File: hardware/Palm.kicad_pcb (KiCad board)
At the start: 2 copper layers, 10 parts, among them J1 Conn_01x02_Female, Q1 IRLML6402, SW1 SW_SPDT, SW2 SW_SPDT, U1 Adafruit_nRF52_Feather, U2 VEML6075_breakout

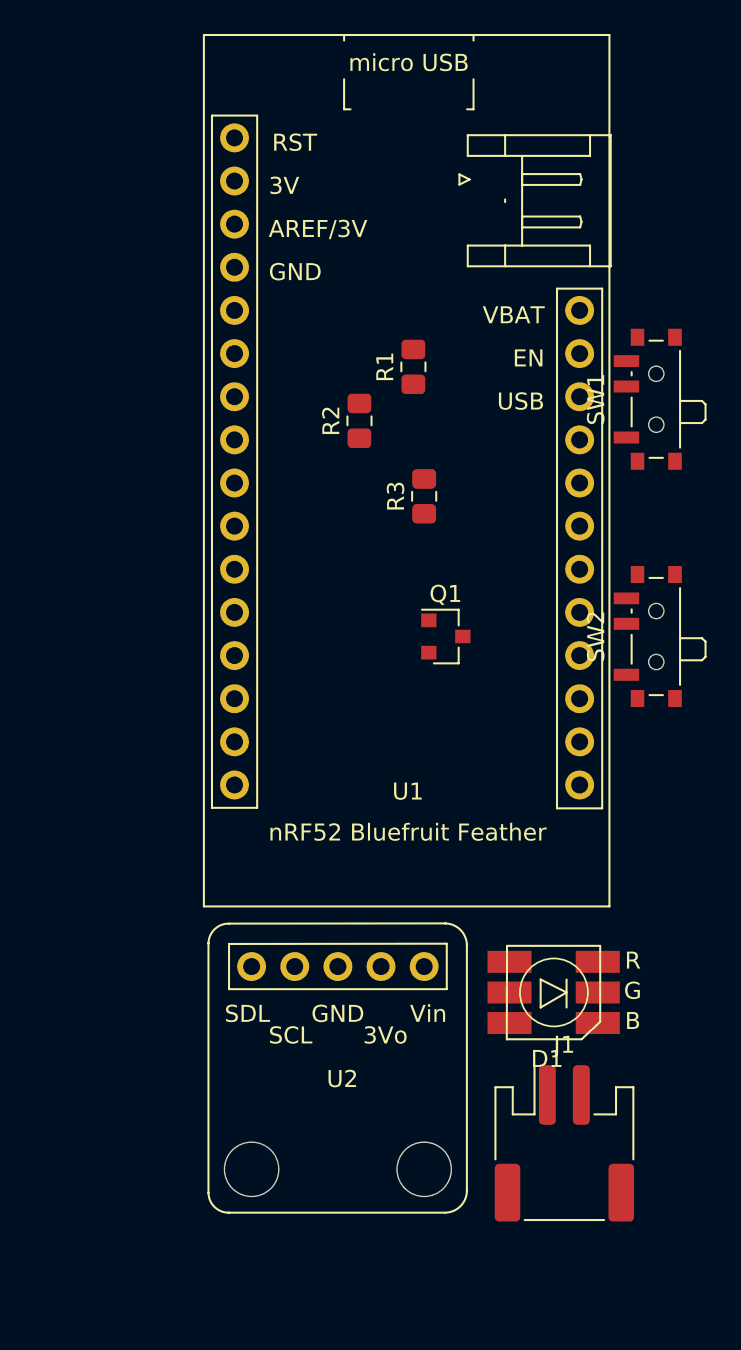
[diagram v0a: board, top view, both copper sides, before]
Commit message: [footprint] Add rats net
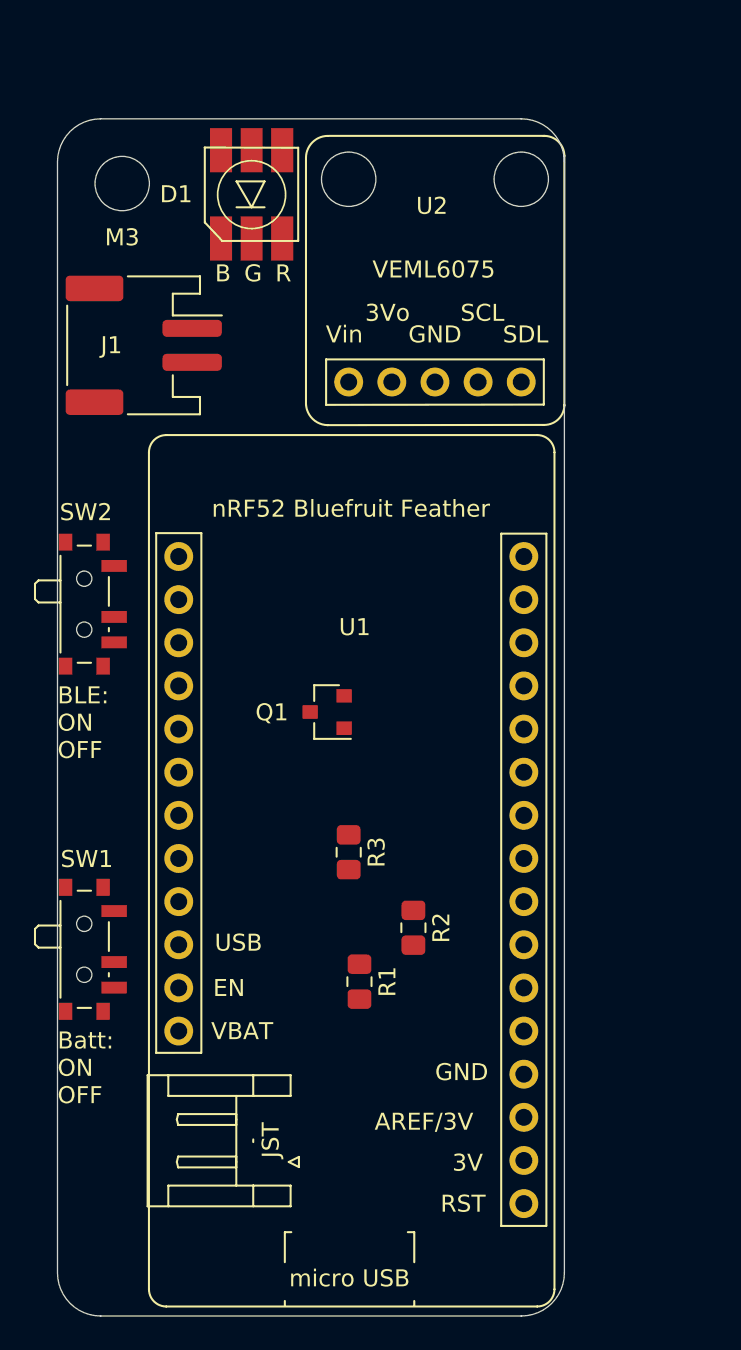
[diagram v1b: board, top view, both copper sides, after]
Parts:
- added M3: Keychain hole, MountingHole:MountingHole_3.2mm_M3, F.Cu at (134.0, 55.2)
- J1: value Conn_01x02_Female -> JST PH2
- moved J1 53.1 mm to (135.3, 64.8), turned to 270 degrees
- moved D1 50.2 mm to (141.6, 55.9), turned to 90 degrees
- moved SW1 46.3 mm to (132.1, 100.3), turned to 270 degrees
- moved U2 45.4 mm to (152.4, 61.6), turned to 0 degrees
- moved R1 36.3 mm to (148.0, 102.2), turned to 270 degrees
- moved SW2 33.1 mm to (132.1, 80.0), turned to 270 degrees
- moved R2 30.0 mm to (151.1, 99.1), turned to 270 degrees
- moved U1 23.9 mm to (147.0, 95.7), turned to 180 degrees
- moved R3 21.4 mm to (147.3, 94.6), turned to 270 degrees
- moved Q1 8.28 mm to (146.1, 86.4), turned to 180 degrees
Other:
- board outline added: 29.8 x 70.5 mm
- board text added: "BLE: ON OFF"
- board text added: "Batt: ON OFF"

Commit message: [footprint] Add back Cu zone with GND
Co-authored-by: Chinmay Pendharkar <notthetup@gmail.com>
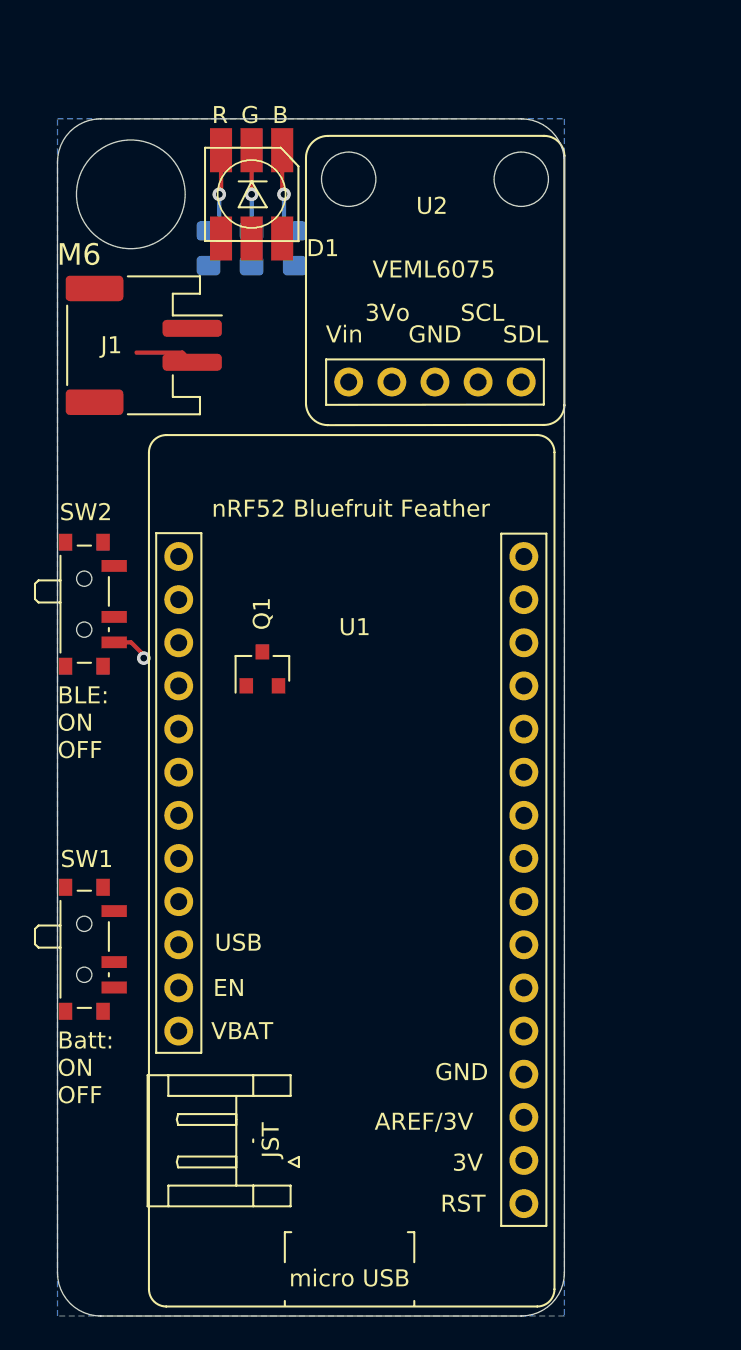
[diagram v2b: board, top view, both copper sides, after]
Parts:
- removed M3: Keychain hole, MountingHole:MountingHole_3.2mm_M3
- added M6: , , F.Cu at (140.0, 57.5)
- R1, R2, R3: moved to B.Cu
- moved R1 43.3 mm to (144.1, 59.1)
- moved R2 41.1 mm to (141.6, 59.1)
- moved R3 36.5 mm to (139.1, 59.1)
- moved Q1 4.58 mm to (142.2, 83.8), turned to 90 degrees
- turned D1 to 270 degrees
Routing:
- net GND: track 0.00 -> 5.75 mm, vias 0 -> 1
- net Net-(D1-Pad3): track 0.00 -> 5.06 mm, vias 0 -> 1
- net Net-(D1-Pad1): track 0.00 -> 5.06 mm, vias 0 -> 1
- net Net-(D1-Pad2): track 0.00 -> 4.75 mm, vias 0 -> 1
- added copper zone on B.Cu, net GND

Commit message: [footprint] Link SDA/SCL and RGB LED tracks
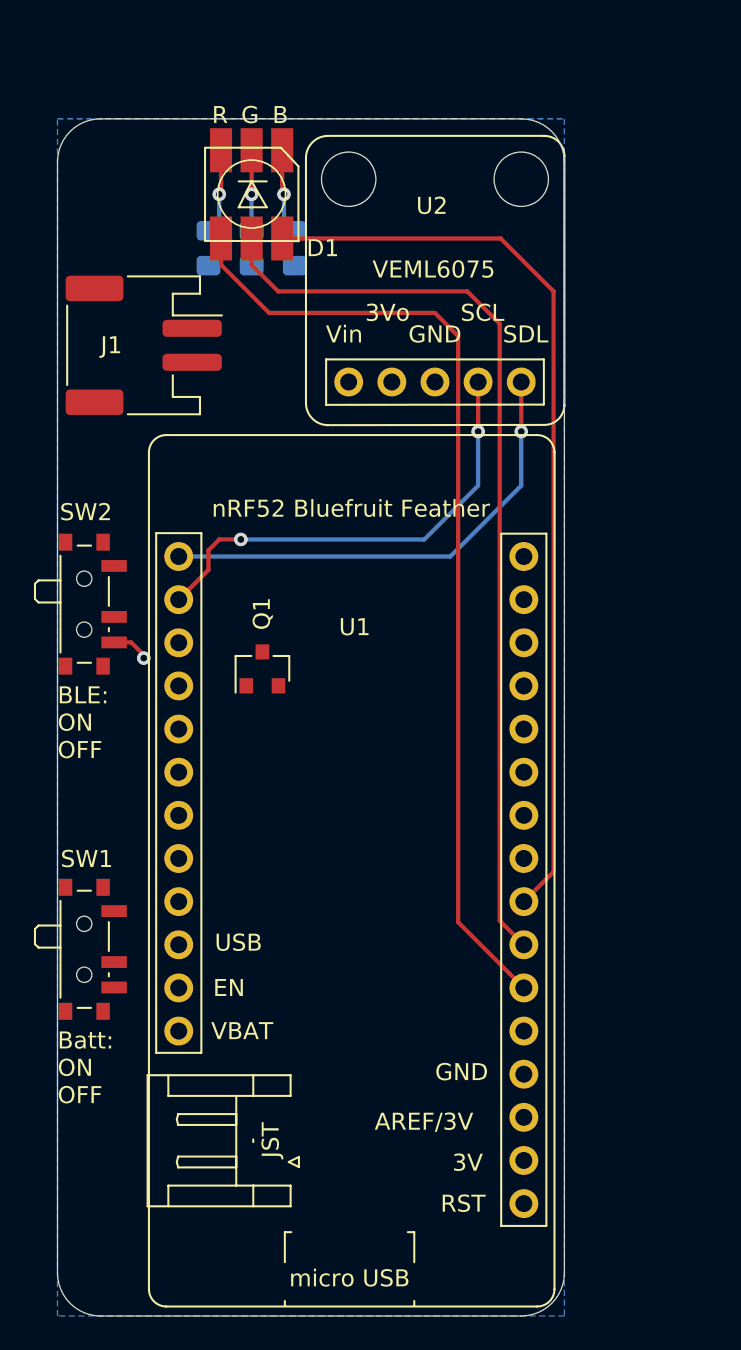
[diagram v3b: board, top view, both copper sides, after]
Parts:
- removed M6: , 
- J1: value JST PH2 -> Conn_01x02_Female
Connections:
- SW1 pad 3: Net-(SW1-Pad3) -> (no net)
- U1 pad 1: Net-(U1-Pad1) -> (no net)
- U1 pad 10: Net-(U1-Pad10) -> (no net)
- U1 pad 11: Net-(U1-Pad11) -> (no net)
- U1 pad 12: Net-(U1-Pad12) -> (no net)
- U1 pad 13: Net-(U1-Pad13) -> (no net)
- U1 pad 14: Net-(U1-Pad14) -> (no net)
- U1 pad 15: Net-(U1-Pad15) -> (no net)
- U1 pad 16: Net-(U1-Pad16) -> (no net)
- U1 pad 19: Net-(U1-Pad19) -> (no net)
- U1 pad 20: Net-(U1-Pad20) -> (no net)
- U1 pad 21: Net-(U1-Pad21) -> (no net)
- U1 pad 22: Net-(U1-Pad22) -> (no net)
- U1 pad 23: Net-(U1-Pad23) -> (no net)
- U1 pad 26: +5V -> (no net)
- U1 pad 27: Net-(U1-Pad27) -> (no net)
- U1 pad 3: Net-(U1-Pad3) -> (no net)
- U1 pad 5: Net-(U1-Pad5) -> (no net)
- U1 pad 6: /RED -> /BLUE
- U1 pad 8: /BLUE -> /RED
- U1 pad 9: Net-(U1-Pad9) -> (no net)
- U2 pad 2: Net-(U2-Pad2) -> (no net)
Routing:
- net /BLUE: track 0.00 -> 57.2 mm
- net /GREEN: track 0.00 -> 54.7 mm
- net /RED: track 0.00 -> 53.9 mm
- net /SDA: track 0.00 -> 28.0 mm, vias 0 -> 1
- net /SCL: track 0.00 -> 27.2 mm, vias 0 -> 2
- net GND: track 5.75 -> 2.23 mm

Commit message: [footprint] Complete footprint layout
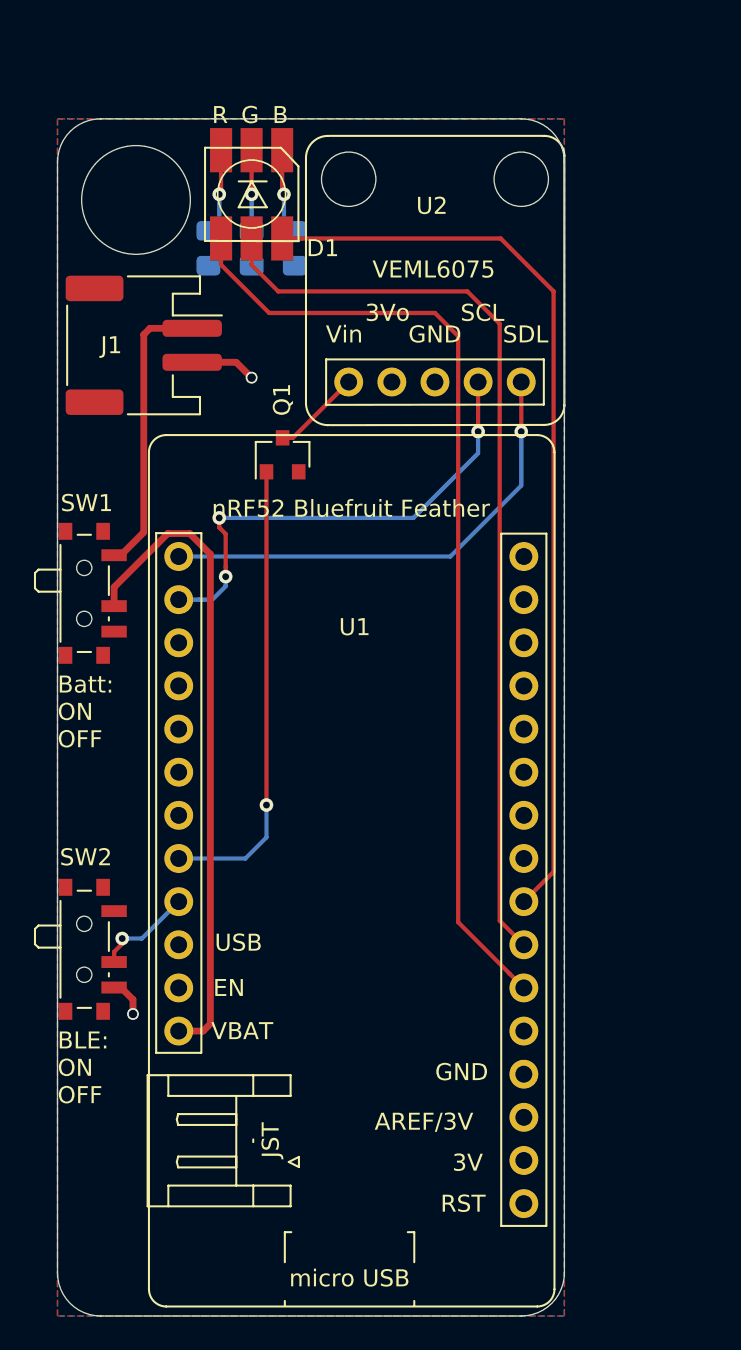
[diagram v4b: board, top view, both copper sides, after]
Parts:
- added ?: , , F.Cu at (135.9, 56.5)
- moved SW1 21.0 mm to (132.1, 79.4)
- moved SW2 20.3 mm to (132.1, 100.3)
- moved Q1 12.7 mm to (143.4, 71.2)
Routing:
- net Net-(SW1-Pad2): track 0.00 -> 38.3 mm
- net /EN_SENSOR: track 0.00 -> 27.2 mm, vias 0 -> 1
- net Net-(J1-Pad1): track 0.00 -> 16.9 mm
- net Net-(SW2-Pad2): track 0.00 -> 5.81 mm, vias 0 -> 1
- net Net-(Q1-Pad3): track 0.00 -> 5.25 mm
- net GND: track 2.23 -> 6.13 mm, vias 1 -> 2
- net /SCL: track 27.2 -> 28.4 mm, vias 2 -> 3
- added copper zone on F.Cu, net +3V3
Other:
- net class Power added: clearance 0.3, trace_width 0.4, via_dia 0.7, via_drill 0.5

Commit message: [footprint] Update footprint layout
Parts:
- moved R1 2.54 mm to (144.1, 61.6)
- moved R2 2.54 mm to (141.6, 61.6)
- moved R3 2.54 mm to (139.1, 61.6)
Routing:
- net Net-(D1-Pad3): track 5.06 -> 7.60 mm
- net Net-(D1-Pad2): track 4.75 -> 7.29 mm
- net Net-(D1-Pad1): track 5.06 -> 7.60 mm
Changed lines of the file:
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@@
     (thickness 1.6)
     (drawings 12)
-    (tracks 83)
+    (tracks 86)
     (zones 0)
     (modules 11)
@@
   )
   (page A4)
+  (title_block
+    (title Palm@Hutscape)
+    (date 2019-06-10)
+    (rev V1.0)
+    (comment 1 "Keychain for measuring UV Index")
+  )
   (layers
     (0 F.Cu signal)
     (31 B.Cu signal)
-    (32 B.Adhes user hide)
+    (32 B.Adhes user)
     (33 F.Adhes user)
-    (34 B.Paste user hide)
+    (34 B.Paste user)
     (35 F.Paste user)
-    (36 B.SilkS user hide)
+    (36 B.SilkS user)
     (37 F.SilkS user)
     (38 B.Mask user)
@@
     (44 Edge.Cuts user)
     (45 Margin user)
-    (46 B.CrtYd user hide)
-    (47 F.CrtYd user hide)
-    (48 B.Fab user hide)
-    (49 F.Fab user hide)
+    (46 B.CrtYd user)
+    (47 F.CrtYd user)
+    (48 B.Fab user)
+    (49 F.Fab user)
   )
   (setup
@@
     (solder_mask_min_width 0.25)
     (aux_axis_origin 74.93 106.045)
-    (visible_elements FFFFFF7F)
+    (visible_elements FFFFFFFF)
     (pcbplotparams
       (layerselection 0x010fc_ffffffff)
@@
     (fp_arc (start 10.414 -24.638) (end 11.43 -24.638) (angle -90) (layer F.SilkS) (width 0.12))
     (fp_arc (start -11.43 -24.638) (end -11.43 -25.654) (angle -90) (layer F.SilkS) (width 0.12))
-    (fp_text user JST (at 4.2545 -15.8623 270) (layer F.SilkS)
+    (fp_text user JST (at 3.4798 -16.0528) (layer F.SilkS)
       (effects (font (size 1 1) (thickness 0.15)))
     )
@@
       (effects (font (size 1 1) (thickness 0.15)))
     )
-    (fp_text user B (at -4.6609 -1.6891) (layer F.SilkS)
-      (effects (font (size 1 1) (thickness 0.15)))
-    )
-    (fp_text user G (at -4.6609 0.0889) (layer F.SilkS)
-      (effects (font (size 1 1) (thickness 0.15)))
-    )
-    (fp_text user R (at -4.6609 1.8669) (layer F.SilkS)
+    (fp_text user B (at -0.508 -1.651) (layer F.SilkS)
+      (effects (font (size 1 1) (thickness 0.15)))
+    )
+    (fp_text user R (at -0.508 1.905) (layer F.SilkS)
       (effects (font (size 1 1) (thickness 0.15)))
     )
@@
   )
   (module Resistor_SMD:R_0805_2012Metric_Pad1.15x1.40mm_HandSolder (layer B.Cu)
-    (at 139.065 59.055 270)
+    (at 139.065 61.595 270)
     (descr "Resistor SMD 0805 (2012 Metric), square (rectangular) end terminal, IPC_7351 nominal with elongated pad for handsoldering. (Body size source: https://docs.google.com/spreadsheets/d/1BsfQQcO9C6DZCsRaXUlFlo91Tg2WpOkGARC1WS5S8t0/edit?usp=sharing), generated with kicad-footprint-generator")
     (tags "resistor handsolder")
     (attr smd)
-    (fp_text reference R3 (at 0 -1.905) (layer B.SilkS)
+    (fp_text reference R3 (at 2.54 0) (layer B.SilkS)
       (effects (font (size 1 1) (thickness 0.15)) (justify mirror))
     )
@@
   )
   (module Resistor_SMD:R_0805_2012Metric_Pad1.15x1.40mm_HandSolder (layer B.Cu)
-    (at 141.605 59.055 270)
+    (at 141.605 61.595 270)
     (descr "Resistor SMD 0805 (2012 Metric), square (rectangular) end terminal, IPC_7351 nominal with elongated pad for handsoldering. (Body size source: https://docs.google.com/spreadsheets/d/1BsfQQcO9C6DZCsRaXUlFlo91Tg2WpOkGARC1WS5S8t0/edit?usp=sharing), generated with kicad-footprint-generator")
     (tags "resistor handsolder")
     (attr smd)
-    (fp_text reference R2 (at 0 -1.905) (layer B.SilkS)
+    (fp_text reference R2 (at 2.54 0) (layer B.SilkS)
       (effects (font (size 1 1) (thickness 0.15)) (justify mirror))
     )
@@
   )
   (module Resistor_SMD:R_0805_2012Metric_Pad1.15x1.40mm_HandSolder (layer B.Cu)
-    (at 144.145 59.055 270)
+    (at 144.145 61.595 270)
     (descr "Resistor SMD 0805 (2012 Metric), square (rectangular) end terminal, IPC_7351 nominal with elongated pad for handsoldering. (Body size source: https://docs.google.com/spreadsheets/d/1BsfQQcO9C6DZCsRaXUlFlo91Tg2WpOkGARC1WS5S8t0/edit?usp=sharing), generated with kicad-footprint-generator")
     (tags "resistor handsolder")
     (attr smd)
-    (fp_text reference R1 (at 0 -1.905) (layer B.SilkS)
+    (fp_text reference R1 (at 2.54 0) (layer B.SilkS)
       (effects (font (size 1 1) (thickness 0.15)) (justify mirror))
     )
@@
     (tags SOT-23)
     (attr smd)
-    (fp_text reference Q1 (at 3.2512 -0.0254 90) (layer F.SilkS)
+    (fp_text reference Q1 (at 2.63652 -0.0254 180) (layer F.SilkS)
       (effects (font (size 1 1) (thickness 0.15)))
     )
@@
   (segment (start 141.605 53.28) (end 141.605 55.88) (width 0.25) (layer F.Cu) (net 1) (status 10))
   (segment (start 141.605 55.88) (end 141.605 58.03) (width 0.25) (layer B.Cu) (net 1) (status 20))
+  (segment (start 141.605 58.03) (end 141.605 60.57) (width 0.25) (layer B.Cu) (net 1))
   (via (at 143.51 55.88) (size 0.8) (drill 0.4) (layers F.Cu B.Cu) (net 2))
   (segment (start 143.405 55.775) (end 143.51 55.88) (width 0.25) (layer F.Cu) (net 2))
@@
   (segment (start 143.51 57.395) (end 144.145 58.03) (width 0.25) (layer B.Cu) (net 2) (status 20))
   (segment (start 143.51 55.88) (end 143.51 57.395) (width 0.25) (layer B.Cu) (net 2))
+  (segment (start 144.145 58.03) (end 144.145 60.57) (width 0.25) (layer B.Cu) (net 2))
   (via (at 134.62 104.14) (size 0.7) (drill 0.5) (layers F.Cu B.Cu) (net 3))
   (segment (start 138.105 65.77) (end 140.7 65.77) (width 0.4) (layer F.Cu) (net 3))
@@
   (segment (start 139.7 57.395) (end 139.065 58.03) (width 0.25) (layer B.Cu) (net 8) (status 20))
   (segment (start 139.7 55.88) (end 139.7 57.395) (width 0.25) (layer B.Cu) (net 8))
+  (segment (start 139.065 58.03) (end 139.065 60.57) (width 0.25) (layer B.Cu) (net 8))
   (segment (start 138.75258 105.1433) (end 137.3124 105.1433) (width 0.4) (layer F.Cu) (net 9))
   (segment (start 139.17676 104.71912) (end 138.75258 105.1433) (width 0.4) (layer F.Cu) (net 9))

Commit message: [footprint] Generate gerbers
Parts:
- added R4: 0R, Resistor_SMD:R_0805_2012Metric_Pad1.15x1.40mm_HandSolder, B.Cu at (148.6, 63.5)
- added REF**: OSHW-Logo_7.5x8mm_SilkScreen, Symbol:OSHW-Logo_7.5x8mm_SilkScreen, B.Cu at (149.2, 88.9)
- moved ? 4.02 mm to (134.6, 60.3)
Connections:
- U2 pad 2: (no net) -> Net-(R4-Pad2)
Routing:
- net Net-(R4-Pad2): track 0.00 -> 3.53 mm
- net Net-(Q1-Pad3): track 5.25 -> 8.78 mm
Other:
- board text added: "Get started at hutscape.com/palm"
- board text added: "Palm@Hutscape V1.0 2019"
